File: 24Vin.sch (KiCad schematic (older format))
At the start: 30 parts, among them J1 Conn_01x02_Male, U3 TPS5430DDA, U4 AMS1117-3.3

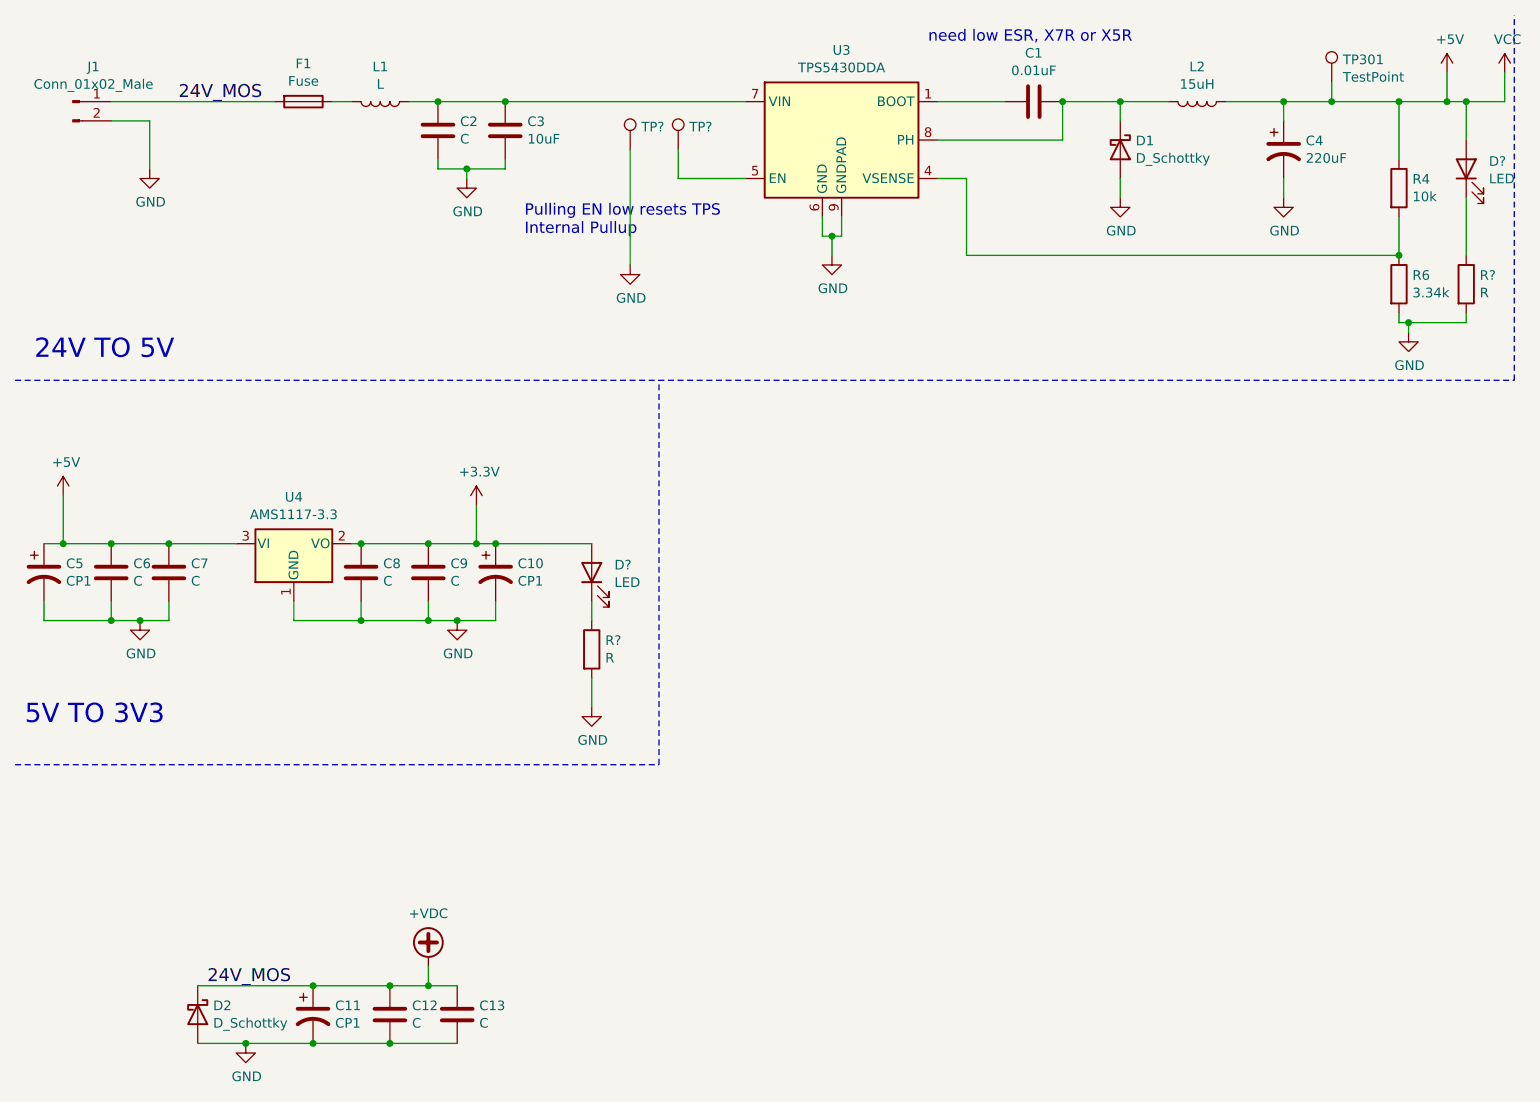
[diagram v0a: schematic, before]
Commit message: connected CoP + mP SPI. pushed updated into layout
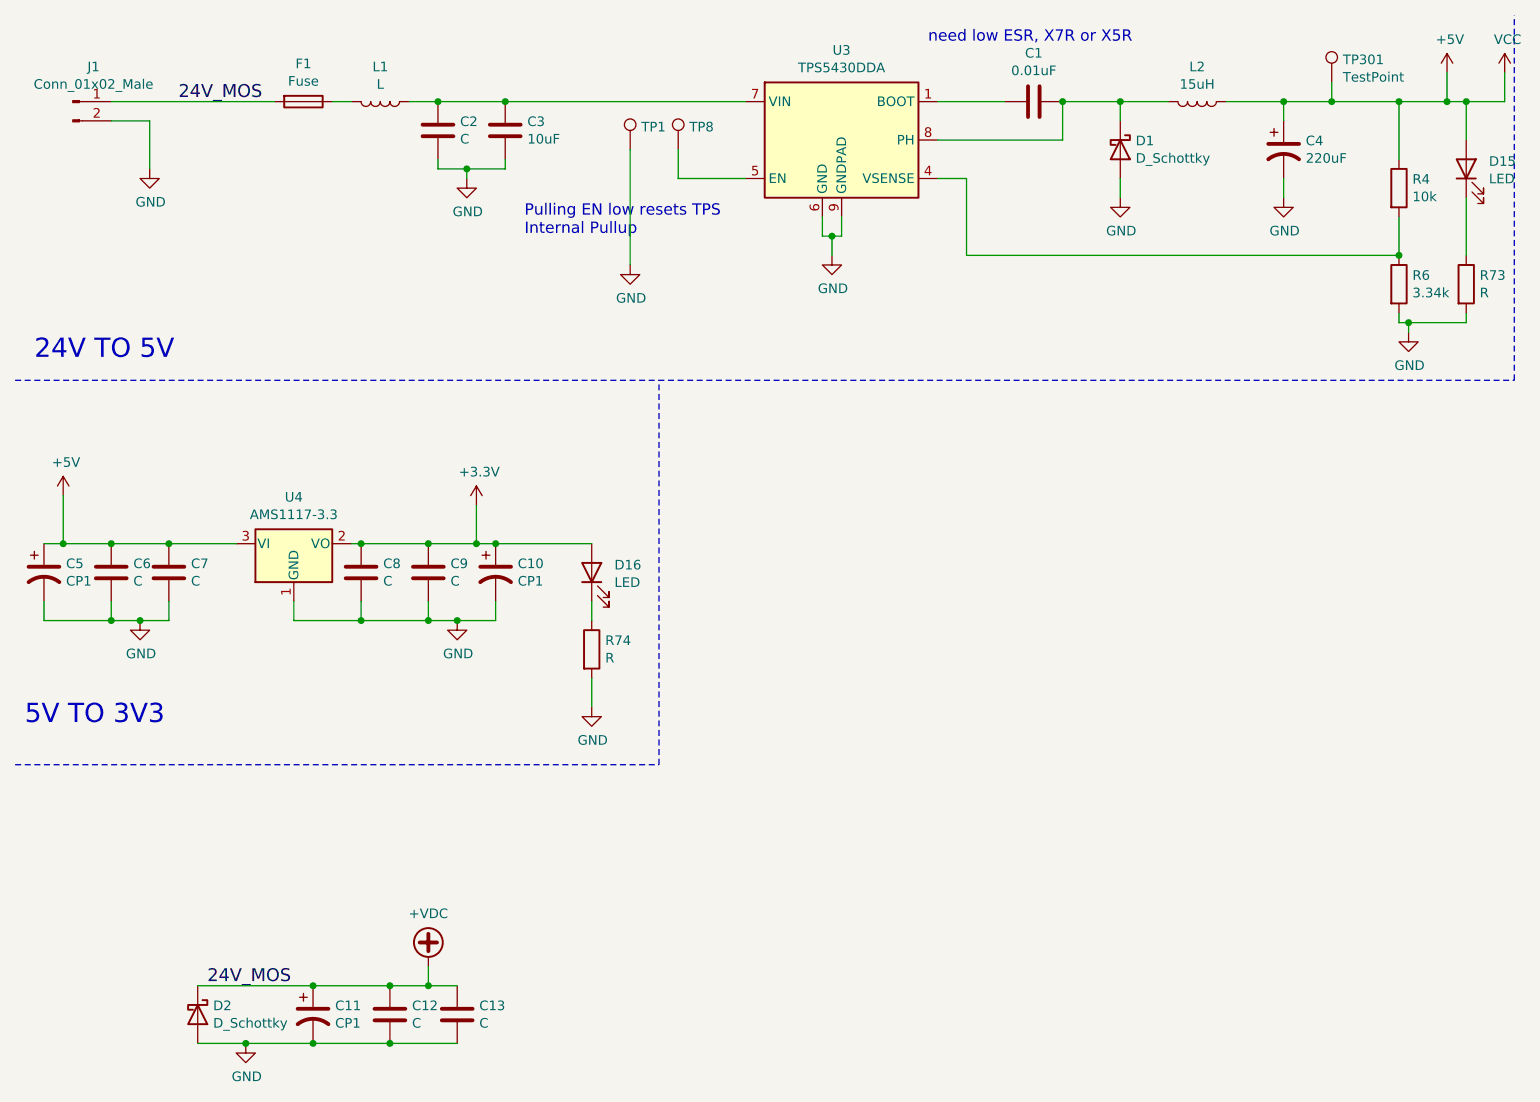
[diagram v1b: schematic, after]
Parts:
- gave numbers to parts that had none: 6
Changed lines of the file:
@@
 need low ESR, X7R or X5R
 $Comp
-L Device:LED D?
+L Device:LED D15
 U 1 1 62235D6D
 P 8150 1350
-F 0 "D?" V 8189 1232 50  0000 R CNN
+F 0 "D15" V 8189 1232 50  0000 R CNN
 F 1 "LED" V 8098 1232 50  0000 R CNN
 F 2 "" H 8150 1350 50  0001 C CNN
@@
 $EndComp
 $Comp
-L Device:R R?
+L Device:R R73
 U 1 1 62236DFE
 P 8150 1950
-F 0 "R?" H 8220 1996 50  0000 L CNN
+F 0 "R73" H 8220 1996 50  0000 L CNN
 F 1 "R" H 8220 1905 50  0000 L CNN
 F 2 "" V 8080 1950 50  0001 C CNN
@@
 	8150 2100 8150 2150
 $Comp
-L Device:LED D?
+L Device:LED D16
 U 1 1 62241ADC
 P 3600 3450
-F 0 "D?" V 3639 3332 50  0000 R CNN
+F 0 "D16" V 3639 3332 50  0000 R CNN
 F 1 "LED" V 3548 3332 50  0000 R CNN
 F 2 "" H 3600 3450 50  0001 C CNN
@@
 $EndComp
 $Comp
-L Device:R R?
+L Device:R R74
 U 1 1 62241AE2
 P 3600 3850
-F 0 "R?" H 3670 3896 50  0000 L CNN
+F 0 "R74" H 3670 3896 50  0000 L CNN
 F 1 "R" H 3670 3805 50  0000 L CNN
 F 2 "" V 3530 3850 50  0001 C CNN
@@
 Connection ~ 3100 3300
 $Comp
-L power:GND #PWR?
+L power:GND #PWR0223
 U 1 1 622485D3
 P 3600 4150
-F 0 "#PWR?" H 3600 3900 50  0001 C CNN
+F 0 "#PWR0223" H 3600 3900 50  0001 C CNN
 F 1 "GND" H 3605 3977 50  0000 C CNN
 F 2 "" H 3600 4150 50  0001 C CNN
@@
 Pulling EN low resets TPS\nInternal Pullup\n
 $Comp
-L Connector:TestPoint TP?
+L Connector:TestPoint TP1
 U 1 1 62264C9C
 P 3800 1250
-F 0 "TP?" H 3858 1368 50  0000 L CNN
+F 0 "TP1" H 3858 1368 50  0000 L CNN
 F 1 "TestPoint" H 3858 1277 50  0001 L CNN
 F 2 "" H 4000 1250 50  0001 C CNN
@@
 $EndComp
 $Comp
-L Connector:TestPoint TP?
+L Connector:TestPoint TP8
 U 1 1 62265545
 P 4050 1250
-F 0 "TP?" H 4108 1368 50  0000 L CNN
+F 0 "TP8" H 4108 1368 50  0000 L CNN
 F 1 "TestPoint" H 4108 1277 50  0001 L CNN
 F 2 "" H 4250 1250 50  0001 C CNN
@@
 	3800 1250 3800 1850
 $Comp
-L power:VCC #PWR?
+L power:VCC #PWR0224
 U 1 1 6226C3B6
 P 8350 850
-F 0 "#PWR?" H 8350 700 50  0001 C CNN
+F 0 "#PWR0224" H 8350 700 50  0001 C CNN
 F 1 "VCC" H 8365 1023 50  0000 C CNN
 F 2 "" H 8350 850 50  0001 C CNN

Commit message: added footprints for most of the c,r, and tp's. need new buck
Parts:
- D15, D16: footprint (none) -> LEDs:LED_0805_HandSoldering
- R4, R6, R73, R74: footprint (none) -> Resistors_SMD:R_0603_HandSoldering
- TP1, TP301, TP8: footprint (none) -> Measurement_Points:Test_Point_Keystone_5015_Micro-Minature
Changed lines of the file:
@@
 EESchema Schematic File Version 4
-EELAYER 30 0
+LIBS:bountifulHarvest-cache
+EELAYER 26 0
 EELAYER END
 $Descr A4 11693 8268
@@
 F 0 "R4" H 7870 1496 50  0000 L CNN
 F 1 "10k" H 7870 1405 50  0000 L CNN
-F 2 "" V 7730 1450 50  0001 C CNN
+F 2 "Resistors_SMD:R_0603_HandSoldering" V 7730 1450 50  0001 C CNN
 F 3 "~" H 7800 1450 50  0001 C CNN
 	1    7800 1450
@@
 F 0 "R6" H 7870 1996 50  0000 L CNN
 F 1 "3.34k" H 7870 1905 50  0000 L CNN
-F 2 "" V 7730 1950 50  0001 C CNN
+F 2 "Resistors_SMD:R_0603_HandSoldering" V 7730 1950 50  0001 C CNN
 F 3 "~" H 7800 1950 50  0001 C CNN
 	1    7800 1950
@@
 F 0 "D15" V 8189 1232 50  0000 R CNN
 F 1 "LED" V 8098 1232 50  0000 R CNN
-F 2 "" H 8150 1350 50  0001 C CNN
+F 2 "LEDs:LED_0805_HandSoldering" H 8150 1350 50  0001 C CNN
 F 3 "~" H 8150 1350 50  0001 C CNN
 	1    8150 1350
@@
 F 0 "R73" H 8220 1996 50  0000 L CNN
 F 1 "R" H 8220 1905 50  0000 L CNN
-F 2 "" V 8080 1950 50  0001 C CNN
+F 2 "Resistors_SMD:R_0603_HandSoldering" V 8080 1950 50  0001 C CNN
 F 3 "~" H 8150 1950 50  0001 C CNN
 	1    8150 1950
@@
 F 0 "D16" V 3639 3332 50  0000 R CNN
 F 1 "LED" V 3548 3332 50  0000 R CNN
-F 2 "" H 3600 3450 50  0001 C CNN
+F 2 "LEDs:LED_0805_HandSoldering" H 3600 3450 50  0001 C CNN
 F 3 "~" H 3600 3450 50  0001 C CNN
 	1    3600 3450
@@
 F 0 "R74" H 3670 3896 50  0000 L CNN
 F 1 "R" H 3670 3805 50  0000 L CNN
-F 2 "" V 3530 3850 50  0001 C CNN
+F 2 "Resistors_SMD:R_0603_HandSoldering" V 3530 3850 50  0001 C CNN
 F 3 "~" H 3600 3850 50  0001 C CNN
 	1    3600 3850
@@
 F 0 "TP301" H 7508 1018 50  0000 L CNN
 F 1 "TestPoint" H 7508 927 50  0000 L CNN
-F 2 "" H 7650 900 50  0001 C CNN
+F 2 "Measurement_Points:Test_Point_Keystone_5015_Micro-Minature" H 7650 900 50  0001 C CNN
 F 3 "~" H 7650 900 50  0001 C CNN
 	1    7450 900
@@
 F 0 "TP1" H 3858 1368 50  0000 L CNN
 F 1 "TestPoint" H 3858 1277 50  0001 L CNN
-F 2 "" H 4000 1250 50  0001 C CNN
+F 2 "Measurement_Points:Test_Point_Keystone_5015_Micro-Minature" H 4000 1250 50  0001 C CNN
 F 3 "~" H 4000 1250 50  0001 C CNN
 	1    3800 1250
@@
 F 0 "TP8" H 4108 1368 50  0000 L CNN
 F 1 "TestPoint" H 4108 1277 50  0001 L CNN
-F 2 "" H 4250 1250 50  0001 C CNN
+F 2 "Measurement_Points:Test_Point_Keystone_5015_Micro-Minature" H 4250 1250 50  0001 C CNN
 F 3 "~" H 4250 1250 50  0001 C CNN
 	1    4050 1250
